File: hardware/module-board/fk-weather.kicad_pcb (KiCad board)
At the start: 2 copper layers, 28.7 x 110.4 mm, 75 parts, among them J1 MICRO-USB, J10 Conn_01x06, J11 Conn_01x06, J2 Conn_01x05, J3 Conn_01x10, J4 Conn_01x04, J5 Conn_01x02, J6 CONN-HDR-2x5, M1 MOUNT_HOLE, M2 MOUNT_HOLE, M3 MOUNT_HOLE, M4 MOUNT_HOLE, Q1 2N7002LT1G, Q2 2N7002LT1G, Q3 2N7002LT1G, Q4 2N7002LT1G, SW1 SPNO, U1 ATSAMD21G18A-AU, U2 MCP1700T-XXX2E, U3 TPS2041B, U4 S25FL1xxK0XM, Y1 FC-135

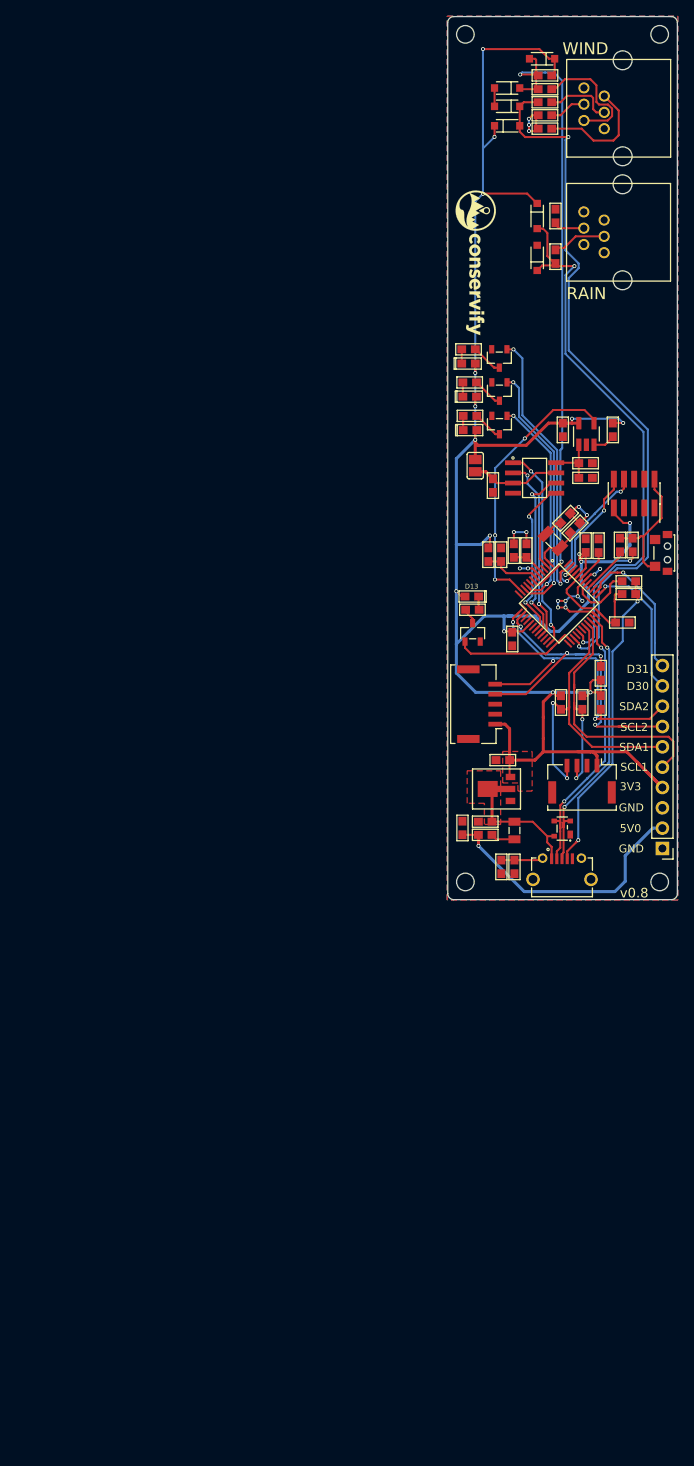
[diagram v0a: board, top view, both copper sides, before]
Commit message: Easier to read labels.
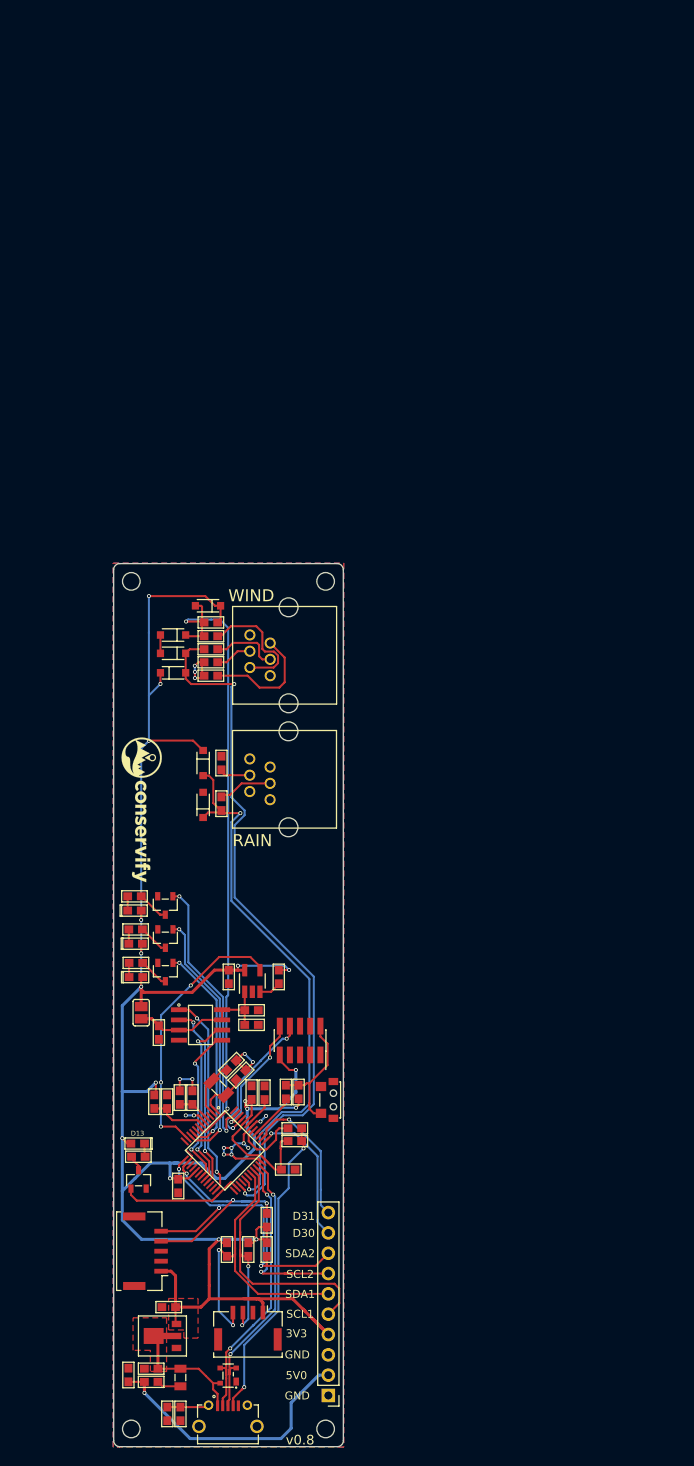
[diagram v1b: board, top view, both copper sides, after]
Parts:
- moved C2 80.1 mm to (99.9, 165.1)
- moved C1 80.1 mm to (98.8, 163.9)
- moved C13 80.1 mm to (98.4, 152.9)
- moved C9 80.1 mm to (85.9, 202.6)
- moved D1 80.1 mm to (86.8, 152.9)
- moved D4 80.1 mm to (98.3, 202.7)
- moved D5 80.1 mm to (87.0, 173.7)
- moved F1 80.1 mm to (92.4, 202.9)
- moved J11 80.1 mm to (105.9, 112.7)
- moved J2 80.1 mm to (88.0, 187.1)
- moved J3 80.1 mm to (110.9, 205.2)
- moved J4 80.1 mm to (100.8, 196.8)
- moved J6 80.1 mm to (107.3, 160.8)
- moved L1 80.1 mm to (88.7, 203.5)
- moved L2 80.1 mm to (89.1, 168.5)
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
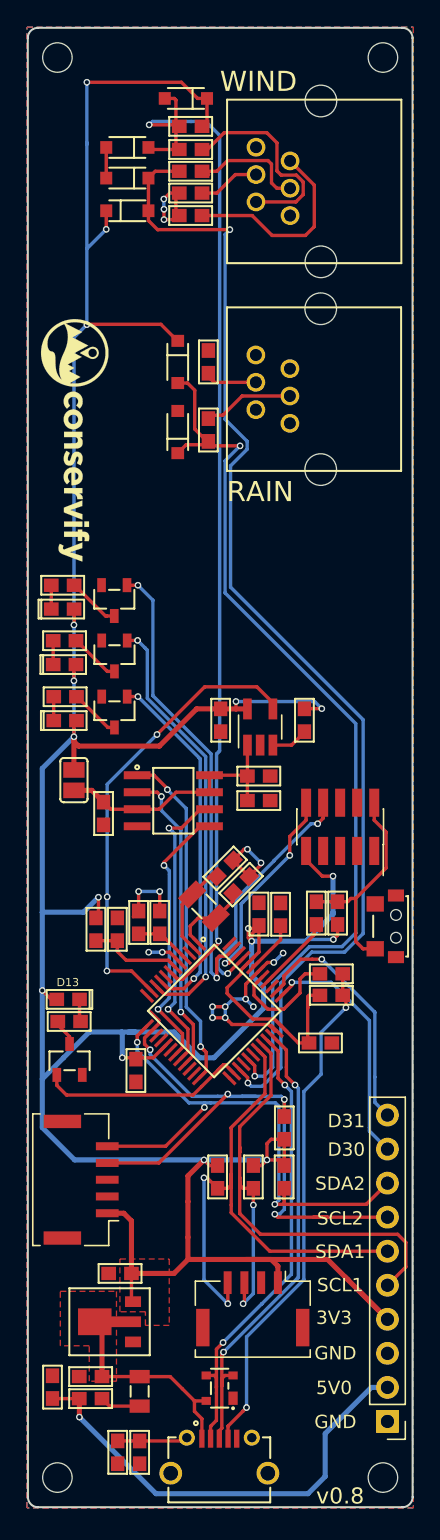
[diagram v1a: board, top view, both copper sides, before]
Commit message: Drop large header. Add debug. Drop LEDs.
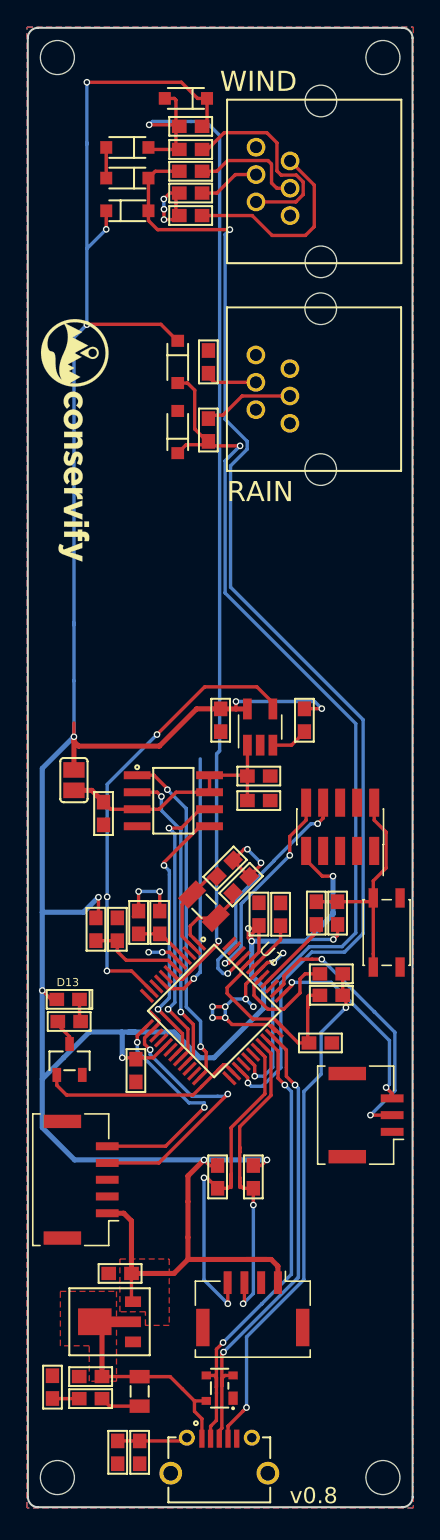
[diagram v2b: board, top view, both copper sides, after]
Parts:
- removed D1: Orange, RocketScreamKicadLibrary:LED-0603
- removed D2: Yellow, RocketScreamKicadLibrary:LED-0603
- removed D3: Blue, RocketScreamKicadLibrary:LED-0603
- removed Q1, Q2, Q3: 2N7002LT1G, RocketScreamKicadLibrary:SOT-23
- removed R1, R3, R5: 2k2, RocketScreamKicadLibrary:RES-0603
- removed R28, R29: 4.7K, RocketScreamKicadLibrary:RES-0603
- C1, C10, C11, C12, C13, C14, C15, C16, C18, C2, C3, C4, C5, C6, C7, C8, C9: footprint RocketScreamKicadLibrary:CAP-0603 -> conservify:CAP-0603
- D10, D11, D6, D7, D8, D9: footprint RocketScreamKicadLibrary:SOD-123 -> conservify:SOD-123
- D4: footprint RocketScreamKicadLibrary:SOT-143B -> conservify:SOT-143B
- D5: footprint RocketScreamKicadLibrary:LED-0603 -> conservify:LED-0603
- F1: footprint RocketScreamKicadLibrary:MF-PSMF020X -> conservify:MF-PSMF020X
- J3: value Conn_01x10 -> CONN_01x03_SERIAL; footprint Socket_Strips:Socket_Strip_Straight_1x10_Pitch2.54mm -> conservify:Molex_CLIK-Mate_502382-0370_1x03_P1.25mm_Vertical
- J6: value CONN-HDR-2x5 -> CONN_02x05_SWD; footprint Socket_Strips:Socket_Strip_Straight_2x05_Pitch1.27mm_SMD -> conservify:HDR_02x05_Pitch1.27mm_SMD_SWD
- L1, L2: footprint RocketScreamKicadLibrary:IND-0603 -> conservify:IND-0603
- M1, M2, M3, M4: footprint RocketScreamKicadLibrary:HOLE_NPTH_2.2MM -> conservify:HOLE_NPTH_2.54MM
- Q4: footprint RocketScreamKicadLibrary:SOT-23 -> conservify:SOT-23
- R10, R11, R17, R2, R22, R23, R30, R31, R32, R33, R34, R4, R6, R7, R8, R9: footprint RocketScreamKicadLibrary:RES-0603 -> conservify:RES-0603
- SW1: footprint RocketScreamKicadLibrary:TS-018 -> conservify:SW_SPST_WURTH_1
- U1: footprint RocketScreamKicadLibrary:TQFP-48_7x7mm_Pitch0.5mm -> conservify:TQFP-48_7x7mm_Pitch0.5mm
- U2: footprint RocketScreamKicadLibrary:SOT-89 -> conservify:SOT-89
- U3: footprint TO_SOT_Packages_SMD:SOT-23-5_HandSoldering -> conservify:SOT-23-5_HandSoldering
- U4: footprint RocketScreamKicadLibrary:SOIC-8-N -> conservify:SOIC-8-N
- Y1: footprint RocketScreamKicadLibrary:ABS07 -> conservify:ABS07
- moved J3 22.9 mm to (109.3, 182.3), turned to 90 degrees
- moved SW1 1.01 mm to (110.8, 168.7)
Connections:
- J3 pad 2: 5V0 -> /D31
- J3 pad 3: GND -> /D30
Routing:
- net /A5: track 35.6 -> 0.00 mm, vias 2 -> 0
- net /A4: track 32.4 -> 0.00 mm, vias 2 -> 0
- net 5V0: track 33.9 -> 2.02 mm, vias 1 -> 0
- net /SCL2: track 47.8 -> 22.4 mm, vias 4 -> 2
- net /SDA2: track 41.4 -> 17.6 mm, vias 3 -> 2
- net 3V3: track 279.5 -> 256.7 mm, vias 17 -> 15
- net /SCL1: track 44.0 -> 24.6 mm
- net /SDA1: track 41.8 -> 26.5 mm
- net /A3: track 26.9 -> 19.6 mm, vias 2 -> 1
- net Net-(Q3-Pad3): track 3.95 -> 0.00 mm
- net Net-(Q2-Pad3): track 3.82 -> 0.00 mm
- net Net-(Q1-Pad3): track 3.78 -> 0.00 mm
- net /D30: track 18.4 -> 15.0 mm, vias 1 -> 2
- net /D31: track 18.3 -> 21.0 mm, vias 1 -> 2
- net Net-(D3-Pad1): track 1.78 -> 0.00 mm
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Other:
- board text removed: "3V3"
- board text removed: "5V0"
- board text removed: "D30"
- board text removed: "D31"
- board text removed: "GND"
- board text removed: "SCL1"
- board text removed: "SCL2"
- board text removed: "SDA1"
- board text removed: "SDA2"

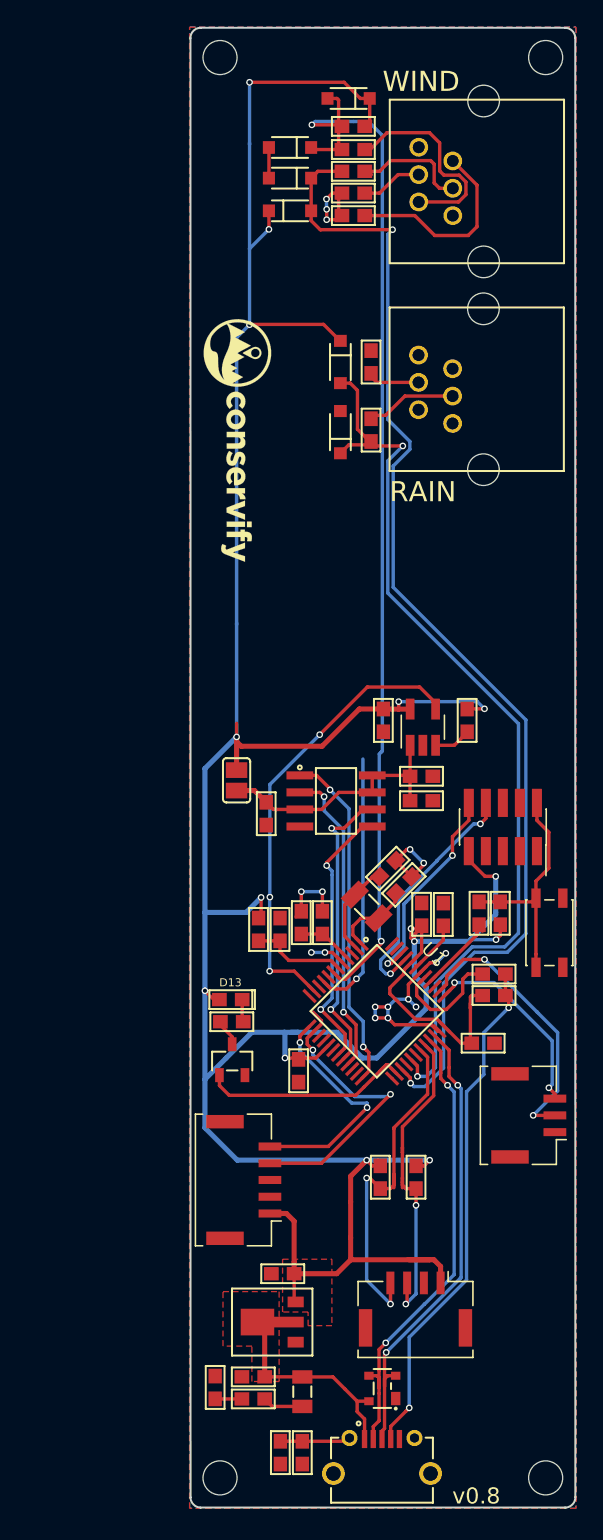
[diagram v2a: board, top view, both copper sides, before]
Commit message: Same size as Core board.
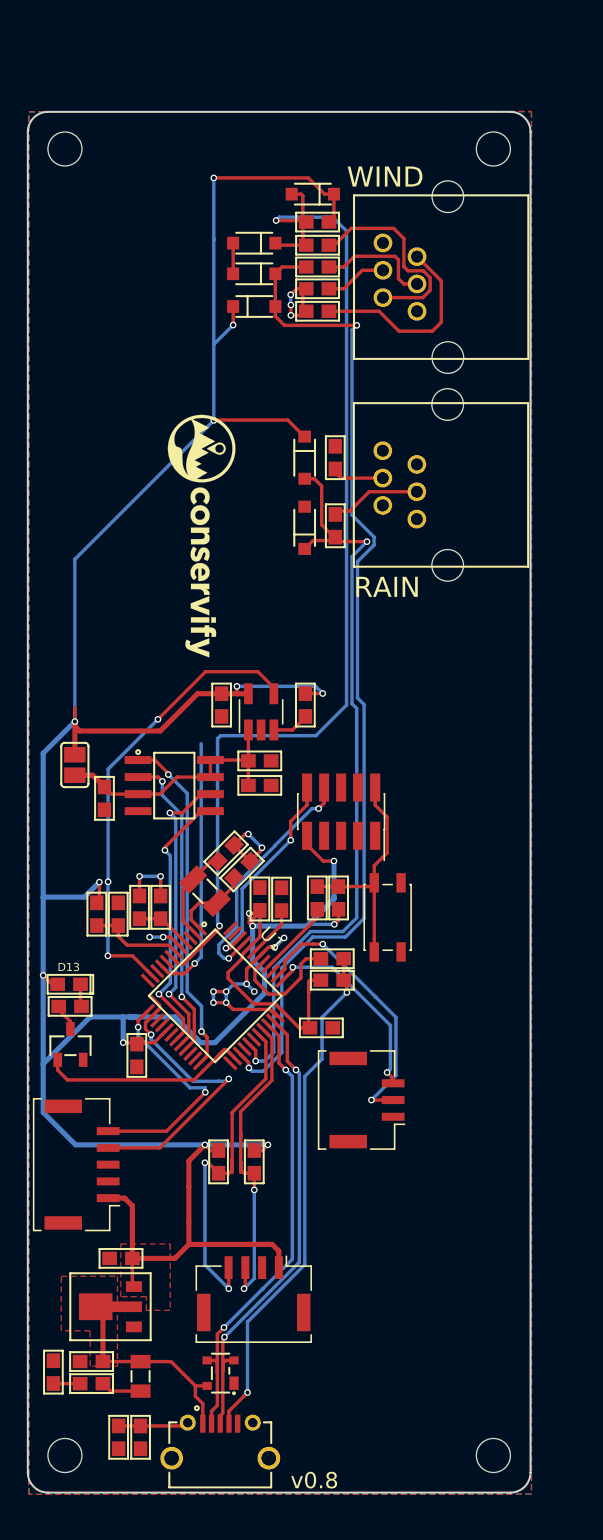
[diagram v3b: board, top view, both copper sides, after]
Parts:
- removed M1, M2, M3, M4: MOUNT_HOLE, conservify:HOLE_NPTH_2.54MM
- added REF**: HOLE_NPTH_2.54MM, conservify:HOLE_NPTH_2.54MM, F.Cu at (74.7, 110.2)
- added REF**: HOLE_NPTH_2.54MM, conservify:HOLE_NPTH_2.54MM, F.Cu at (74.7, 207.7)
- added REF**: HOLE_NPTH_2.54MM, conservify:HOLE_NPTH_2.54MM, F.Cu at (106.6, 207.7)
- added REF**: HOLE_NPTH_2.54MM, conservify:HOLE_NPTH_2.54MM, F.Cu at (106.6, 110.2)
- moved C12 12.1 mm to (78.9, 193.0)
- moved J1 12.1 mm to (86.3, 206.8)
- moved Q4 12.1 mm to (75.1, 177.0)
- moved R8 12.1 mm to (94.6, 172.2)
- moved R9 12.1 mm to (94.6, 170.6)
- moved U1 12.1 mm to (85.9, 173.4)
- moved Y1 12.1 mm to (85.1, 165.6)
- moved C1 12.1 mm to (86.7, 162.8)
- moved C10 12.1 mm to (78.7, 206.3)
- moved C11 12.1 mm to (76.7, 200.7)
- moved C13 12.1 mm to (86.4, 151.7)
- moved C14 12.1 mm to (80.2, 166.8)
- moved C15 12.1 mm to (89.2, 157.7)
- moved C16 12.1 mm to (89.2, 155.9)
- moved C18 12.1 mm to (77.6, 158.7)
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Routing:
- net /WIND_SPEED: track 88.2 -> 76.0 mm
- net /RAIN: track 68.9 -> 56.7 mm
- net 3V3: track 256.7 -> 252.1 mm
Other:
- board size 28.7 x 110.4 mm -> 37.5 x 103 mm

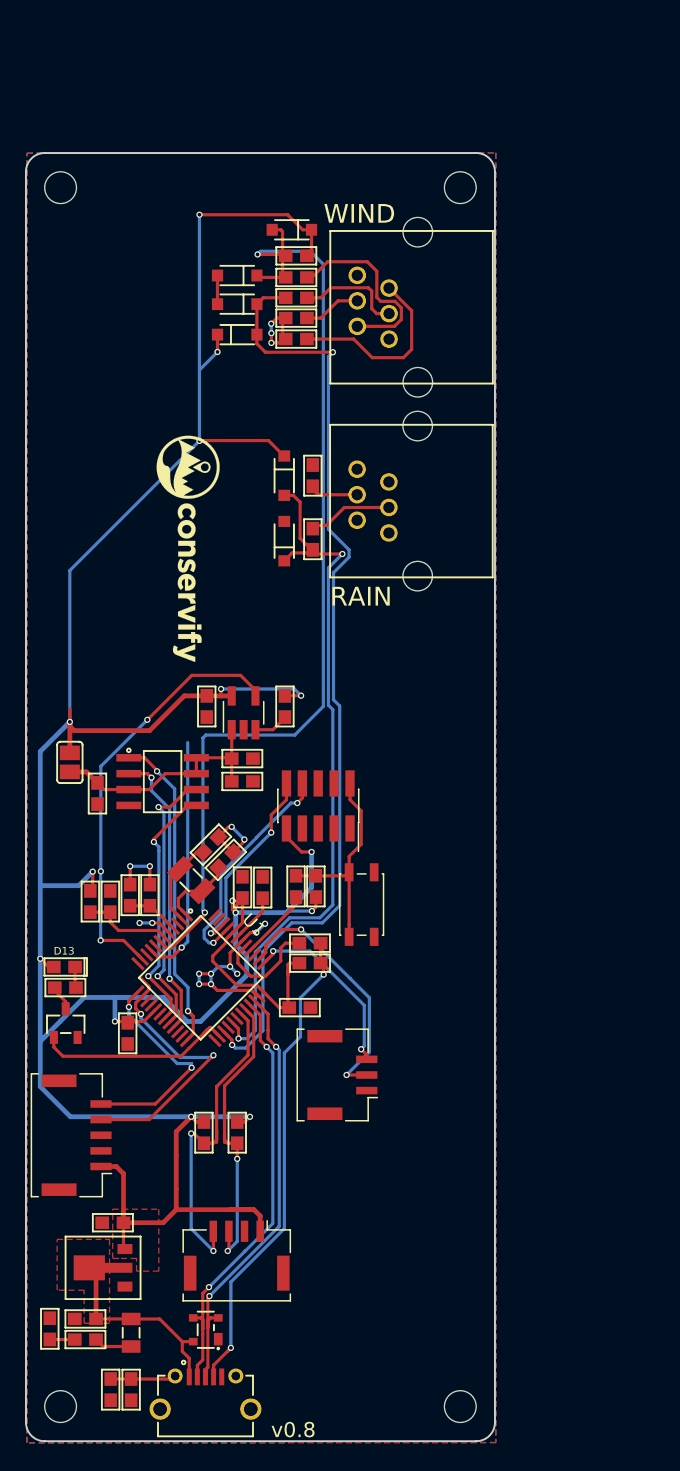
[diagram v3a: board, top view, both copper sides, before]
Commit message: Add RTC. Molex connector cleanup. Add RGB LED.Fix diode footprints.
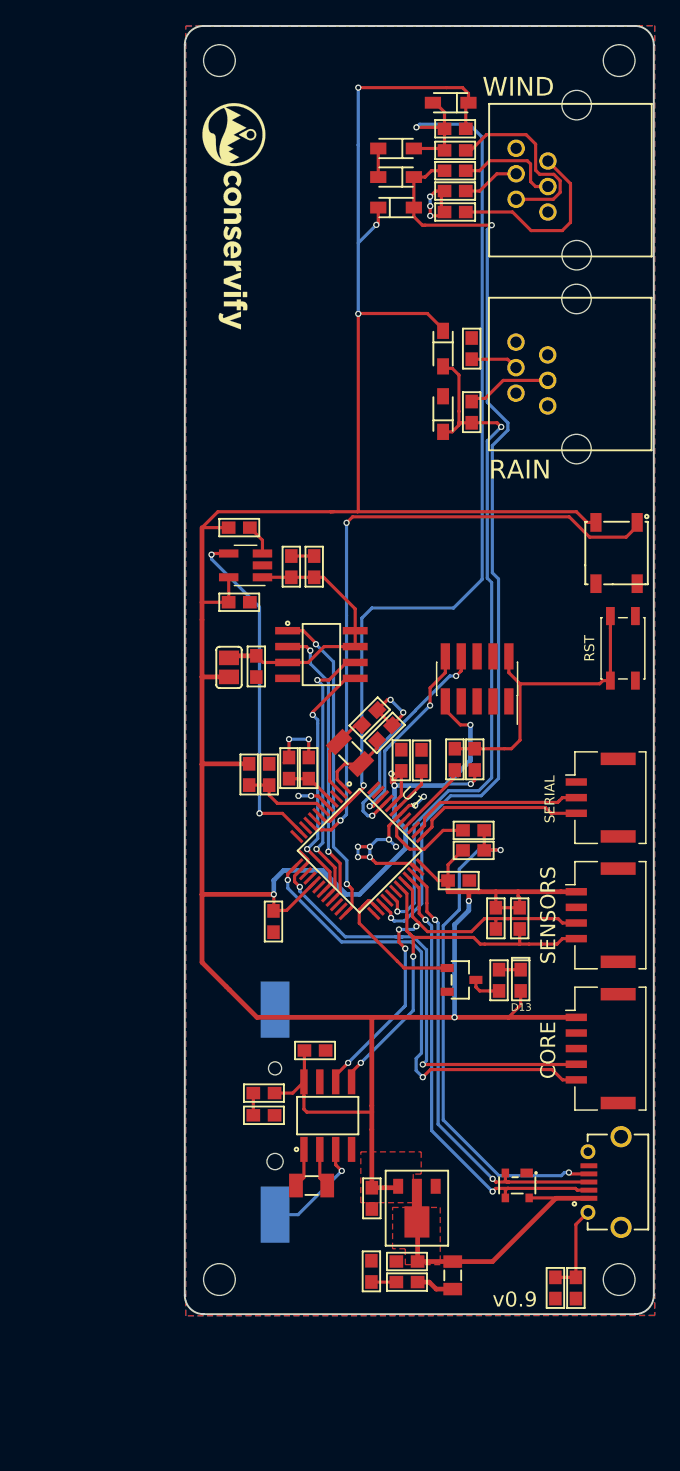
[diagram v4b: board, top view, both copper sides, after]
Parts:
- removed the REF** at (74.7, 110.2)
- removed the REF** at (74.7, 207.7)
- removed the REF** at (106.6, 207.7)
- removed the REF** at (106.6, 110.2)
- added BT1: BATTERY_CELL, conservify:BAT_CR1210, B.Cu at (91.8, 184.2)
- added C17: 10nF, conservify:CAP-0603, F.Cu at (95.0, 179.2)
- added C19: 10nF, conservify:CAP-0603, F.Cu at (90.9, 184.4)
- added R1: 1K, conservify:RES-0603, F.Cu at (90.9, 182.6)
- added REF**: HOLE_NPTH_2.54MM, conservify:HOLE_NPTH_2.54MM, F.Cu at (87.4, 100.1)
- added REF**: HOLE_NPTH_2.54MM, conservify:HOLE_NPTH_2.54MM, F.Cu at (87.4, 197.5)
- added REF**: HOLE_NPTH_2.54MM, conservify:HOLE_NPTH_2.54MM, F.Cu at (119.3, 197.5)
- added REF**: HOLE_NPTH_2.54MM, conservify:HOLE_NPTH_2.54MM, F.Cu at (119.3, 100.1)
- added U5: SK6812, conservify:SK6812, F.Cu at (119.1, 139.4)
- added U6: PCF8523, conservify:SOIC-8-N, F.Cu at (96.0, 184.4)
- added Y2: FC-135, conservify:ABS07, F.Cu at (94.7, 190.0)
- moved J2 42.5 mm to (117.9, 179.1), turned to 270 degrees
- moved J4 39.9 mm to (117.9, 168.4), turned to 270 degrees
- moved D5 36.5 mm to (111.5, 173.6), turned to 270 degrees
- moved C10 36.5 mm to (114.2, 198.2)
- moved R10 36.5 mm to (115.9, 198.2)
- moved J1 36.3 mm to (118.4, 189.7), turned to 90 degrees
- moved R17 34.7 mm to (109.7, 173.6), turned to 270 degrees
- moved Q4 31.8 mm to (106.7, 173.6), turned to 270 degrees
- moved R6 30.5 mm to (111.4, 168.7)
- moved J3 30.3 mm to (117.9, 159.0), turned to 270 degrees
- moved SW1 29.3 mm to (119.6, 147.1)
- moved D4 27.4 mm to (111.2, 190.0), turned to 180 degrees
- moved R7 26.9 mm to (109.5, 168.7)
- moved G*** 26.8 mm to (88.5, 112.5)
- moved C11 26.1 mm to (102.4, 196.1)
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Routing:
- net 3V3: track 252.1 -> 285.4 mm, vias 15 -> 10
- net /A3: track 19.6 -> 52.1 mm, vias 1 -> 2
- net /SDA2: track 17.6 -> 38.2 mm
- net /SCL2: track 22.4 -> 38.2 mm
- net /SCL1: track 24.6 -> 34.8 mm, vias 2 -> 4
- net Net-(BT1-Pad1): track 0.00 -> 8.71 mm, vias 0 -> 1
- net /RST: track 17.4 -> 25.1 mm
- net /D31: track 21.0 -> 14.1 mm, vias 2 -> 0
- net /SDA1: track 26.5 -> 33.3 mm
- net VUSB: track 17.1 -> 23.9 mm
- net /PERIPH_EN: track 34.2 -> 27.7 mm, vias 3 -> 2
- net /D13: track 15.9 -> 12.0 mm
- net Net-(U6-Pad1): track 0.00 -> 3.15 mm
- net Net-(U6-Pad2): track 0.00 -> 3.13 mm
- net /PERIPH_3V3: track 19.5 -> 22.4 mm
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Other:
- board text added: "CORE"
- board text added: "RST"
- board text added: "SENSORS"
- board text added: "SERIAL"
- board text added: "v0.9"
- board text removed: "v0.8"
